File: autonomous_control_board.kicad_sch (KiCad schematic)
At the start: 0 parts

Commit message: Added ESP32 Breakout, Brake Controls (L298N), Throttle Digipot (MCP4231)
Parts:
- added J1, J2: Conn_01x15, Connector_PinSocket_2.54mm:PinSocket_1x15_P2.54mm_Vertical, symbol Connector_Generic:Conn_01x15
- added J3: Screw_Terminal_01x02, symbol Connector:Screw_Terminal_01x02
- added U1: L298N, Package_TO_SOT_THT:TO-220-15_P2.54x5.08mm_StaggerOdd_Lead4.58mm_Vertical, symbol Driver_Motor:L298N
- added U2: MCP4231T-502E/ST, TSSOP14_MC_MCH, symbol ul_MCP4231T-502E-ST:MCP4231T-502E_ST
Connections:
- new net: J3.1 (Pin_1), U1.2 (OUT1)
- new net: J3.2 (Pin_2), U1.3 (OUT2)
- new net +12V: U1.4 (Vs)
- new net +3V3: J2.1 (Pin_1)
- new net +5V: J1.15 (Pin_15), U1.9 (Vss)
- new net CS: J2.8 (Pin_8), U2.1
- new net EN: J1.1 (Pin_1)
- new net EnableA: J1.5 (Pin_5), U1.6 (EnA)
- new net GND: J1.14 (Pin_14), J2.2 (Pin_2), U1.8 (GND)
- new net GPIO1: J2.13 (Pin_13)
- new net GPIO12: J1.12 (Pin_12)
- new net GPIO13: J1.13 (Pin_13)
- new net GPIO14: J1.11 (Pin_11)
- new net GPIO15: J2.3 (Pin_3)
- new net GPIO16: J2.6 (Pin_6)
- new net GPIO17: J2.7 (Pin_7)
- new net GPIO18: J2.9 (Pin_9), U2.2
- new net GPIO19: J2.10 (Pin_10), U2.13
- new net GPIO2: J2.4 (Pin_4)
- new net GPIO21: J2.11 (Pin_11)
- new net GPIO22: J2.14 (Pin_14)
- new net GPIO23: J2.15 (Pin_15), U2.3
- new net GPIO25: J1.8 (Pin_8)
- new net GPIO26: J1.9 (Pin_9)
- new net GPIO27: J1.10 (Pin_10)
- new net GPIO3: J2.12 (Pin_12)
- new net GPIO32: J1.6 (Pin_6), U1.7 (IN2)
- new net GPIO33: J1.7 (Pin_7), U1.5 (IN1)
- new net GPIO34: J1.4 (Pin_4)
- new net GPIO36: J1.2 (Pin_2)
- new net GPIO39: J1.3 (Pin_3)
- new net GPIO4: J2.5 (Pin_5)
- new net SHDN: U2.12
- new net Throttle+: U2.7
- new net Throttle-: U2.6
- new net Vdd: U2.14
- new net Vss: U2.4
- new net WP: U2.11
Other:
- note added: "Brake Controls L298N Motor Driver"
- note added: "DigiPot"
- note added: "ESP32 Breakout Headers"
- note added: "ESP32-Wroom-32 ESP32-Devkit-V1"
- note added: "Linear Actuator"
- note added: "Throttle Control MCP4231 Digital Potentiometer"

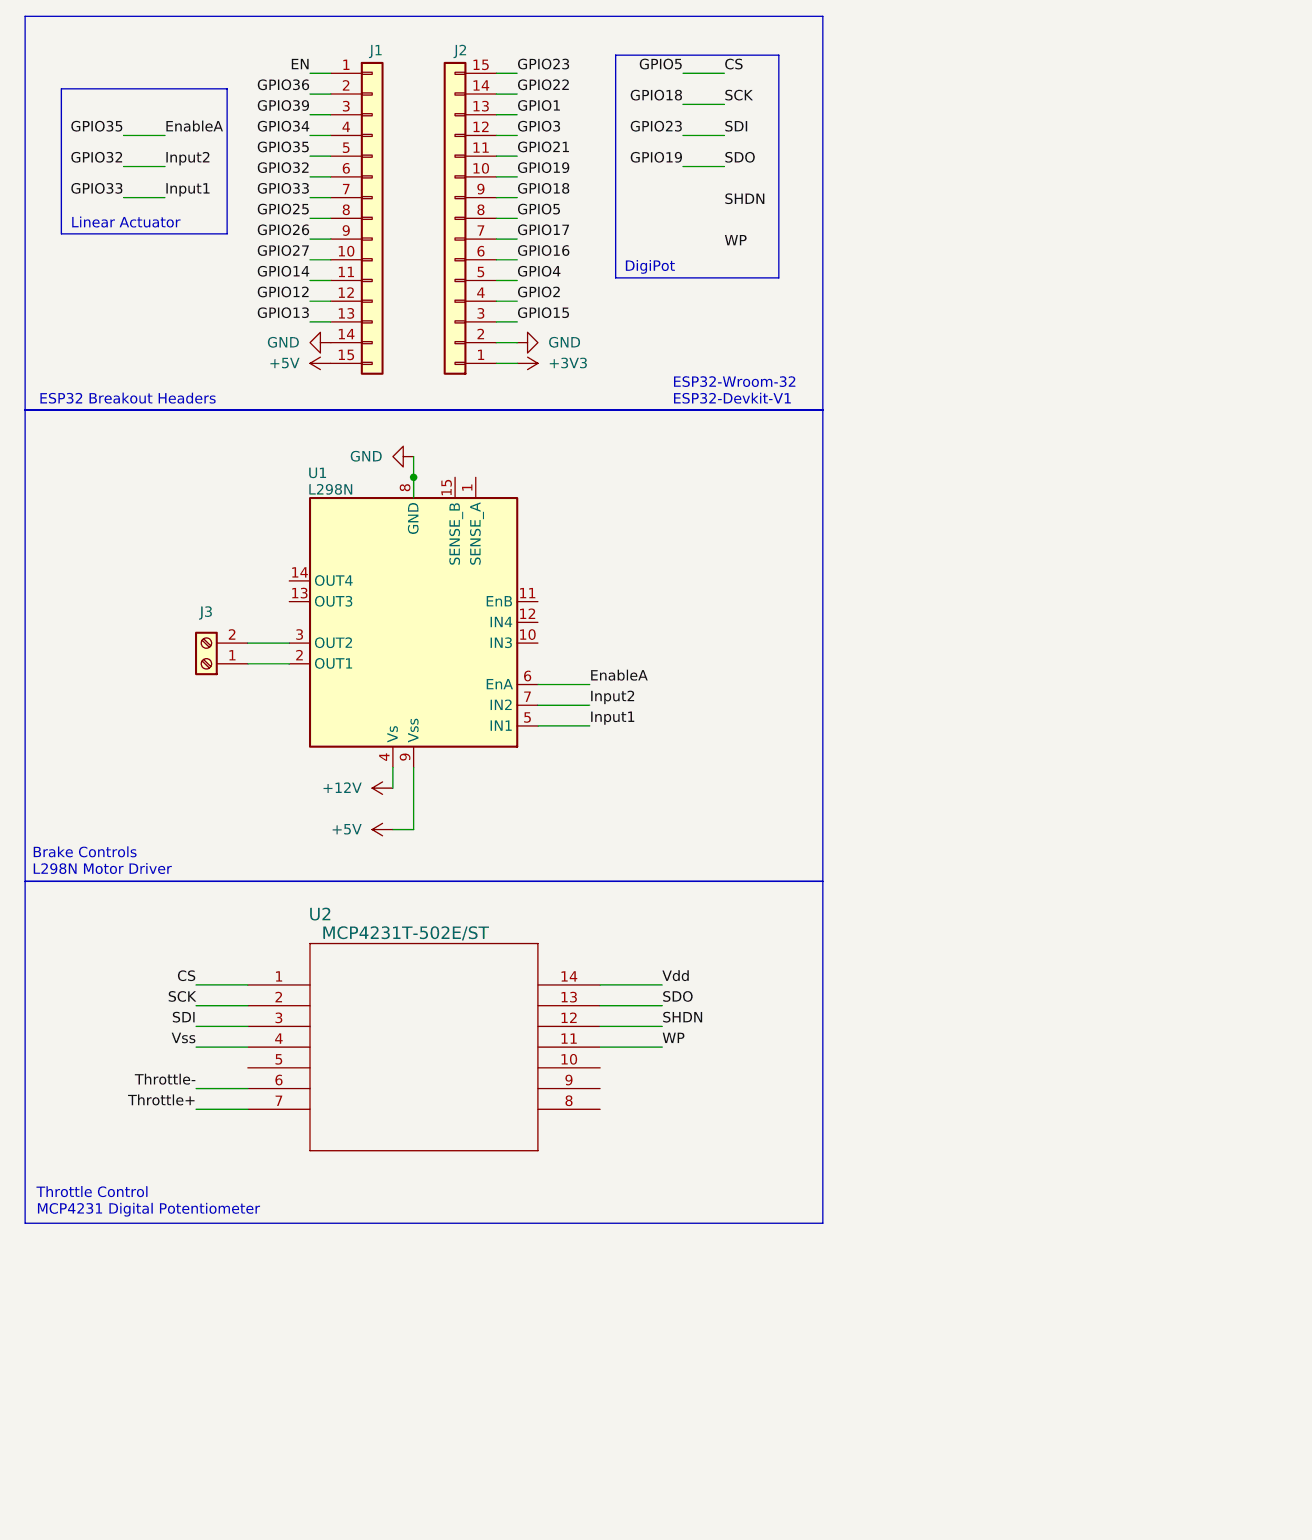
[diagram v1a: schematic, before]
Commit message: Added: Steering Control, Power Distribution (opting for commercial buck convertor)
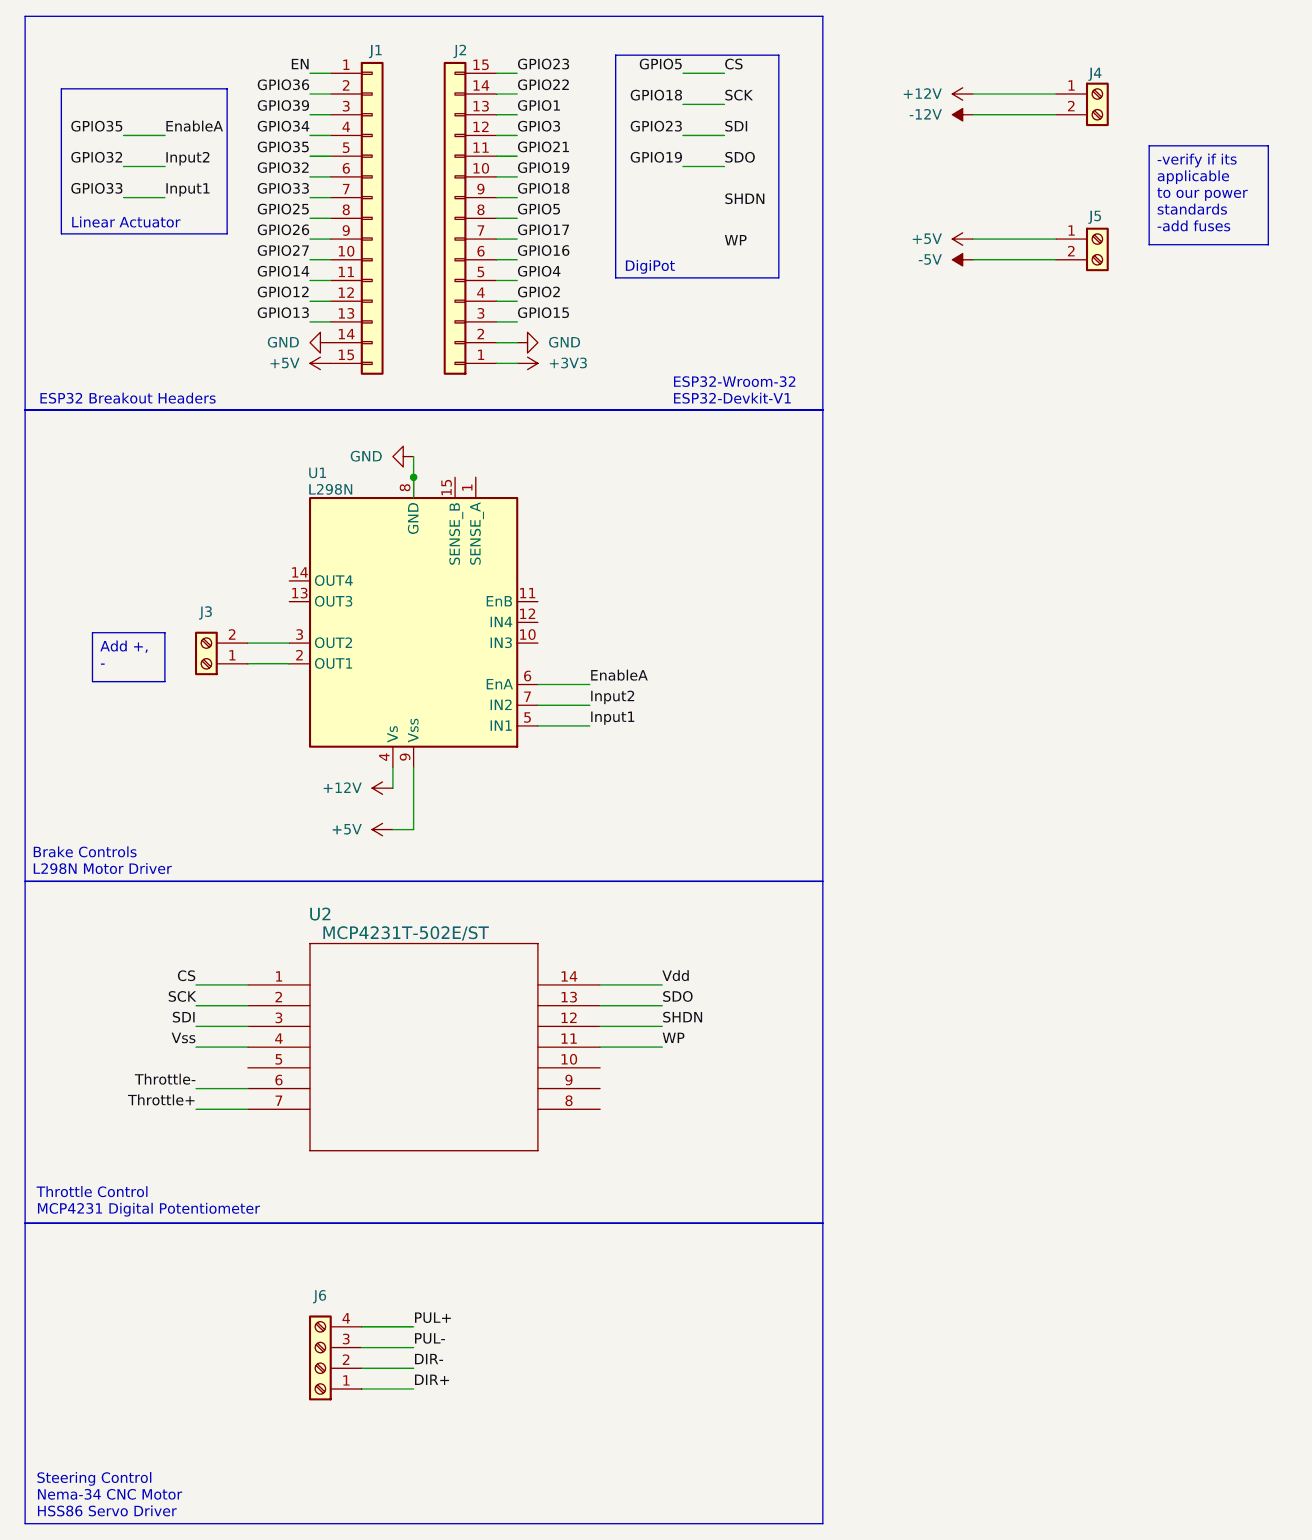
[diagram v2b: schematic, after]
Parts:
- added J4, J5: Screw_Terminal_01x02, symbol Connector:Screw_Terminal_01x02
- added J6: Screw_Terminal_01x04, symbol Connector:Screw_Terminal_01x04
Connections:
- net +12V: now also J4.1 (Pin_1)
- net +5V: now also J5.1 (Pin_1)
- new net -12V: J4.2 (Pin_2)
- new net -5V: J5.2 (Pin_2)
- new net DIR+: J6.1 (Pin_1)
- new net DIR-: J6.2 (Pin_2)
- new net PUL+: J6.4 (Pin_4)
- new net PUL-: J6.3 (Pin_3)
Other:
- note added: "Steering Control Nema-34 CNC Motor HSS86 Servo Driver"

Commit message: Started PCB design. Swapped out the right DigiPot
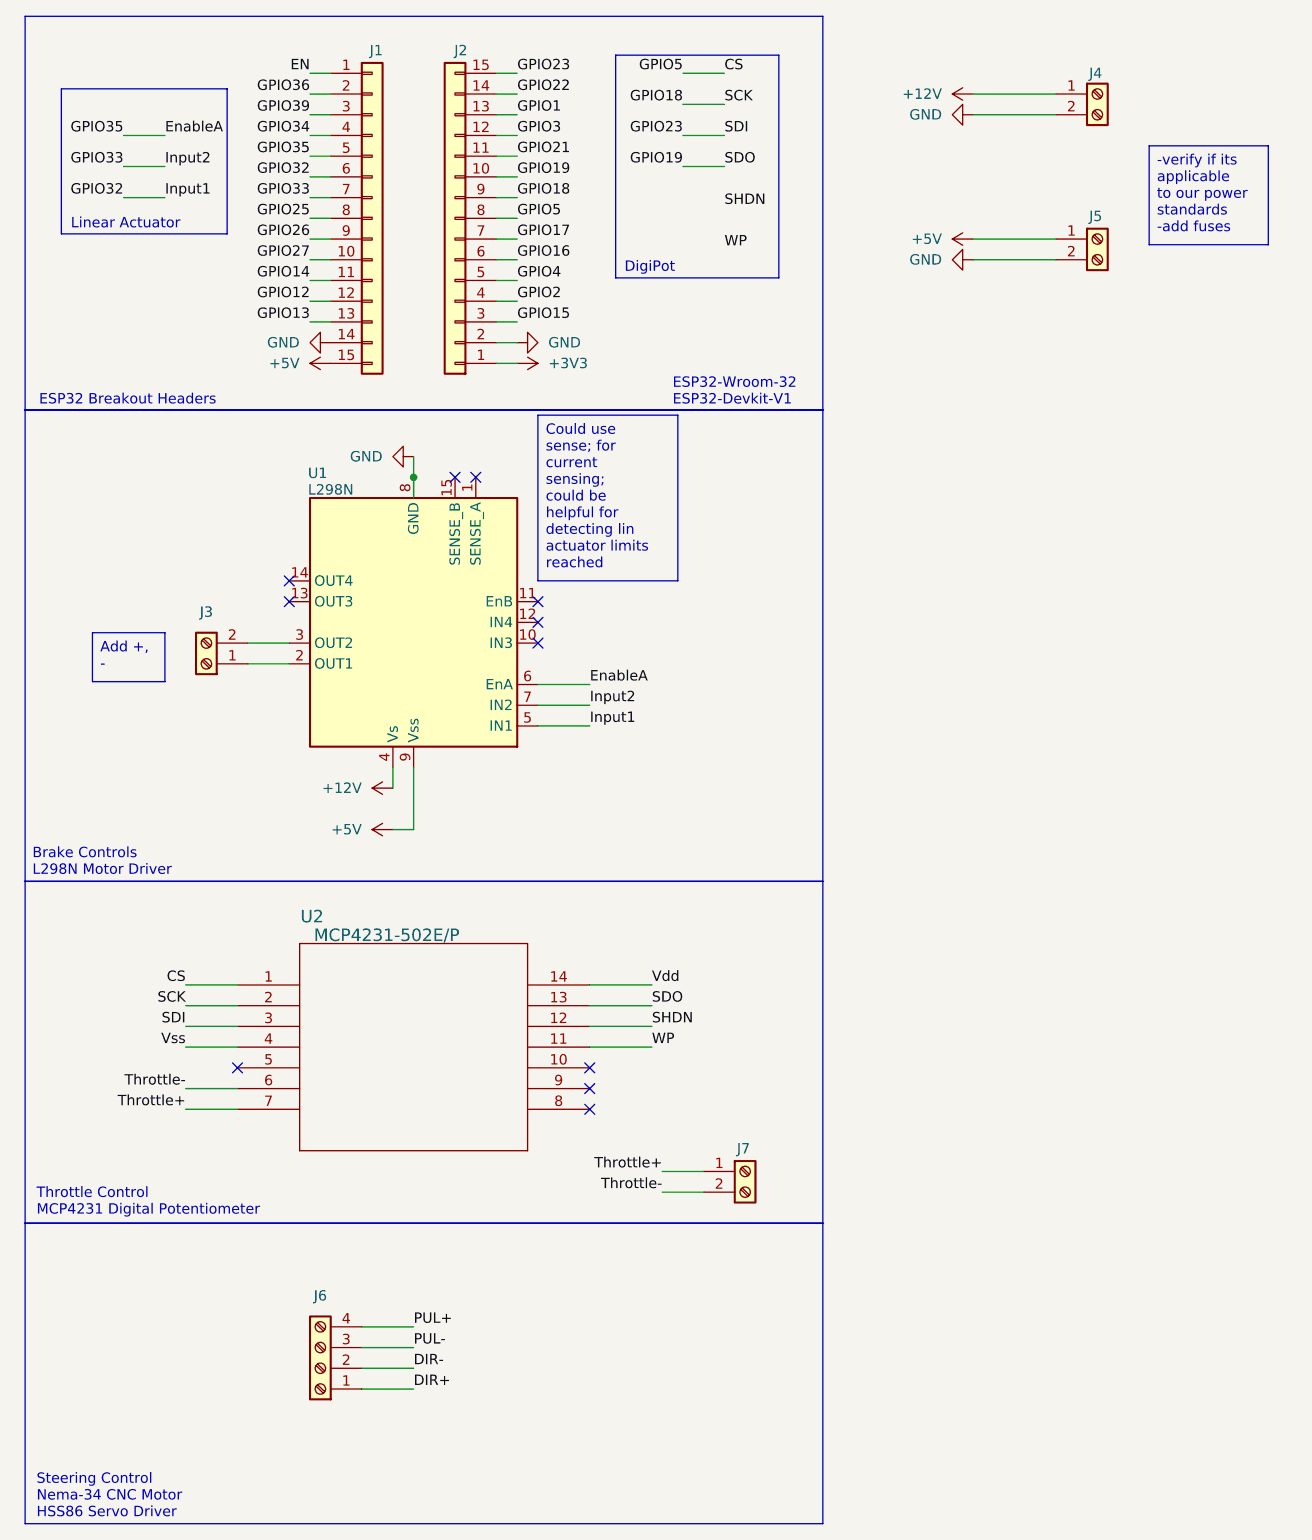
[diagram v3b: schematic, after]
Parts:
- removed U2: MCP4231T-502E/ST, TSSOP14_MC_MCH, symbol ul_MCP4231T-502E-ST:MCP4231T-502E_ST
- added J7: Screw_Terminal_01x02, TerminalBlock_Phoenix:TerminalBlock_Phoenix_MPT-0,5-2-2.54_1x02_P2.54mm_Horizontal, symbol Connector:Screw_Terminal_01x02
- added U2: MCP4231-502E/P, Package_DIP:DIP-14_W7.62mm, symbol MCP4231-502E/P:MCP4231-502E_P
- J3, J4, J5: footprint (none) -> TerminalBlock_Phoenix:TerminalBlock_Phoenix_MPT-0,5-2-2.54_1x02_P2.54mm_Horizontal
- J6: footprint (none) -> TerminalBlock_Phoenix:TerminalBlock_Phoenix_MPT-0,5-4-2.54_1x04_P2.54mm_Horizontal
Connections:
- net -12V is gone; now on net GND: J4.2 (Pin_2)
- net -5V is gone; now on net GND: J5.2 (Pin_2)
- net CS: now also U2.1
- net GPIO18: now also U2.2
- net GPIO19: now also U2.13
- net GPIO23: now also U2.3
- net GPIO32: now also U1.5 (IN1); no longer U1.7 (IN2)
- net GPIO33: now also U1.7 (IN2); no longer U1.5 (IN1)
- net SHDN: now also U2.12
- net Throttle+: now also J7.1 (Pin_1), U2.7
- net Throttle-: now also J7.2 (Pin_2), U2.6
- net Vdd: now also U2.14
- net Vss: now also U2.4
- net WP: now also U2.11
- no-connect marks 0 -> 11
